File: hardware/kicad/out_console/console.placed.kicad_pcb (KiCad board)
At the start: 2 copper layers, 115 x 96 mm, 53 parts, among them J1 RaspberryPi_Pico_SMD_HandSold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, J10 JST_XH_B2B-XH-A_1x02_P2.50mm_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, J11 JST_XH_B2B-XH-A_1x02_P2.50mm_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, J12 JST_XH_B2B-XH-A_1x02_P2.50mm_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, J13 JST_XH_B2B-XH-A_1x02_P2.50mm_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, J14 JST_XH_B2B-XH-A_1x02_P2.50mm_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, J15 JST_XH_B2B-XH-A_1x02_P2.50mm_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, J16 JST_XH_B2B-XH-A_1x02_P2.50mm_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, J17 JST_XH_B2B-XH-A_1x02_P2.50mm_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, J18 JST_XH_B2B-XH-A_1x02_P2.50mm_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, J19 JST_XH_B2B-XH-A_1x02_P2.50mm_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, J2 IDC-Header_2x20_P2.54mm_Verti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, J20 JST_XH_B3B-XH-A_1x03_P2.50mm_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, J21 JST_XH_B3B-XH-A_1x03_P2.50mm_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, J22 PinHeader_2x04_P2.54mm_Vertic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, J3 JST_XH_B4B-XH-A_1x04_P2.50mm_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, J4 JST_XH_B3B-XH-A_1x03_P2.50mm_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, J5 JST_XH_B2B-XH-A_1x02_P2.50mm_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, J6 JST_XH_B8B-XH-A_1x08_P2.50mm_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, J7 JST_XH_B3B-XH-A_1x03_P2.50mm_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, J8 JST_XH_B2B-XH-A_1x02_P2.50mm_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, U1 DIP-14_W7.62mm, U2 DIP-6_W7.62mm

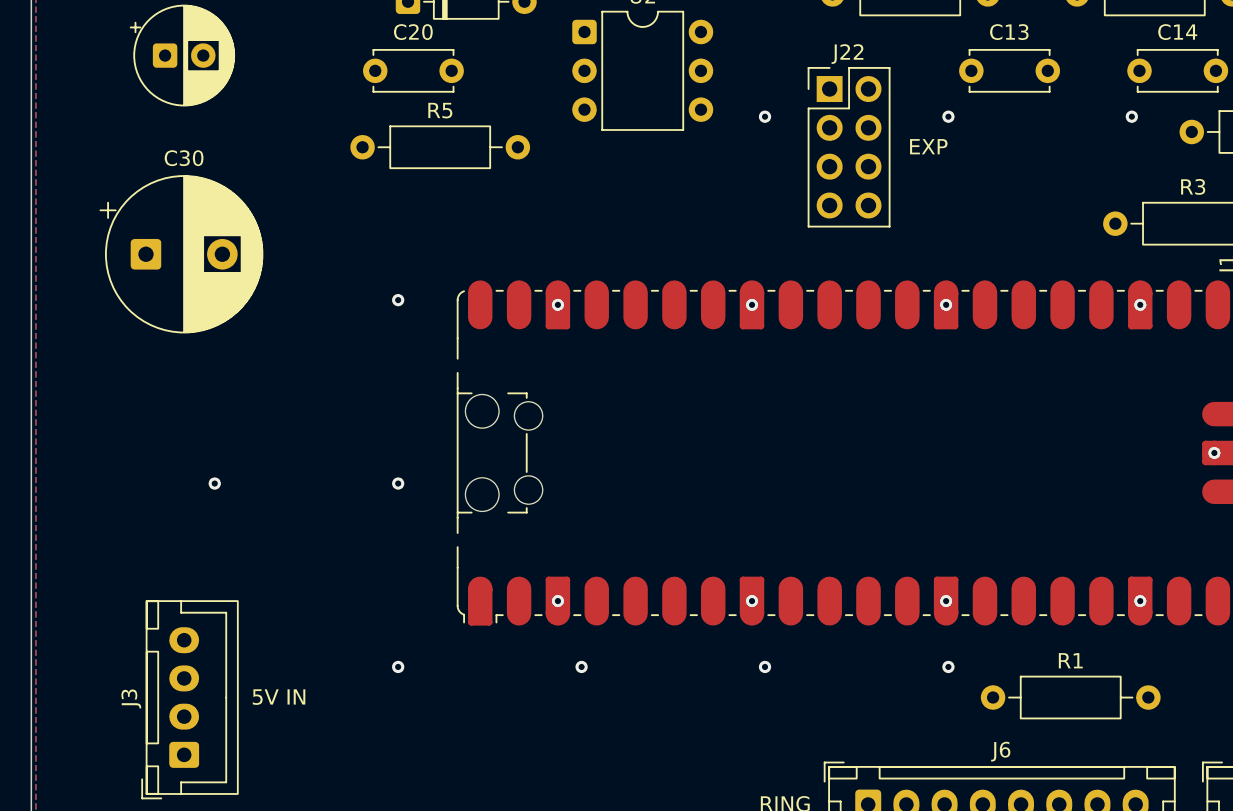
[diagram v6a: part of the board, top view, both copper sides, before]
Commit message: fix(hardware): the four electrical blockers from the pre-fab review
- ENCODER LEVELS. ring_board.py pulled ENC_A/ENC_B up to its 5 V rail; those land
  on GP13/GP14, whose absolute maximum is 3.6 V. Correct when the far end was
  main_board.py's 5 V Pro Micro, wrong from the day it became a Pico. The pull-ups
  move to this board at 3V3 (and ENC_SW gains the one it never had). New
  PICO_LEVELS gate: PI_LEVELS only ever guarded the Pi, so no check on either
  board could see this.
- PI 5 V. Header pins 2/4 are no longer connected. Tying them put the external
  buck in hard parallel with the Pi 5's PMIC rail with no ORing diode, and after
  the rail merge it put the whole WS2812 load on the Pi's 5 V pin -- which
  segno_console_shopping_list.md forbids in as many words. Gated.
- POWER BUTTON. GPIO3 wakes a Pi 4, not a Pi 5, where the GPIO sits behind RP1
  and the PMIC owns power-on. The button passes through to the Pi's own J2 solder
  pads via J9. The old gate asserted the false version and enforced it all design.
- CTRL REFERENCE. One 1k per jack, not one shared. Shared, a TS footswitch in
  either jack pulled the other jack's pot top to ground.

Also: track width 0.2 -> 0.6 mm (Freerouting reads widths from the DSN netclass,
so TRACK_W/TRACK_PWR were decorative and +5V carried ~1 A on 0.5 A copper);
export() refuses to plot a board with no tracks; --severity-all everywhere.

Refs #747
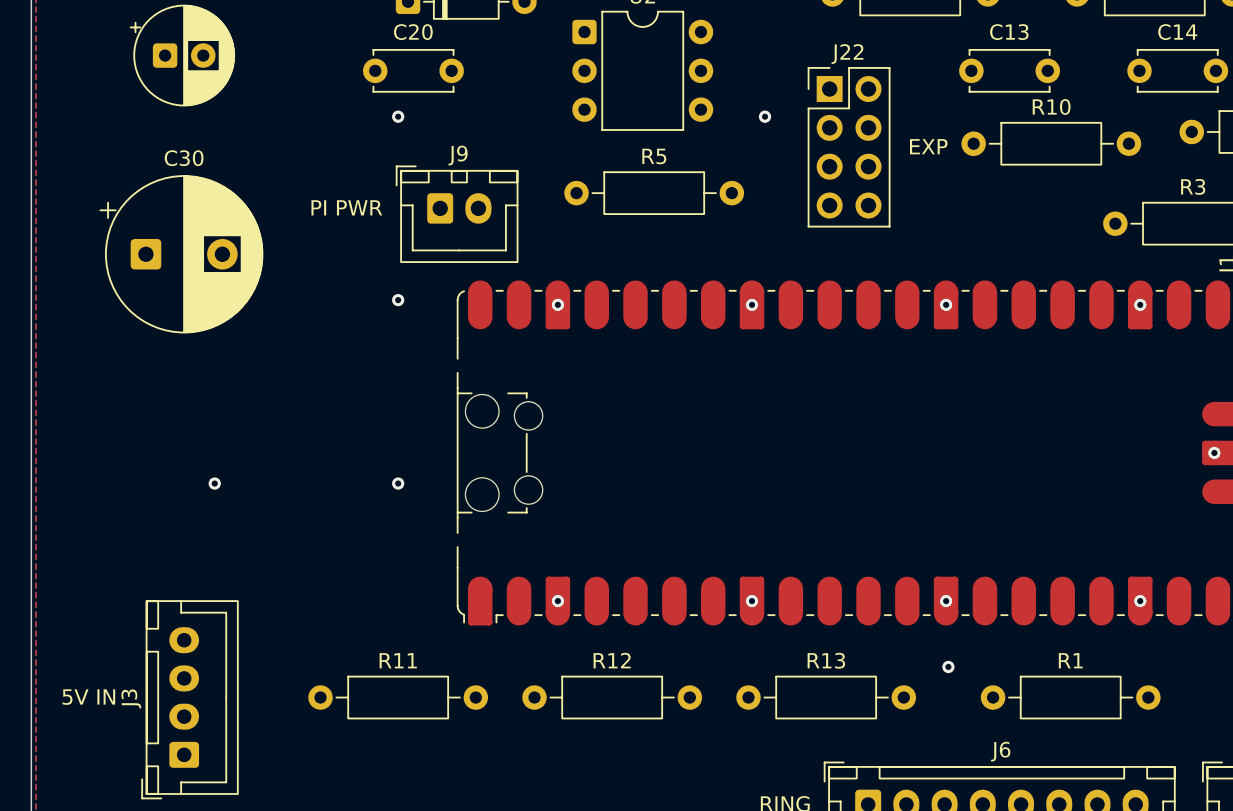
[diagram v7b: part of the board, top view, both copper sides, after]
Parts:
- added J9: JST_XH_B2B-XH-A_1x02_P2.50mm_Vertical, JST_XH_B2B-XH-A_1x02_P2.50mm_Vertical, F.Cu at (126.8, 90.0)
- added R10: R_Axial_DIN0207_L6.3mm_D2.5mm_P10.16mm_Horizontal, R_Axial_DIN0207_L6.3mm_D2.5mm_P10.16mm_Horizontal, F.Cu at (161.7, 85.8)
- added R11: R_Axial_DIN0207_L6.3mm_D2.5mm_P10.16mm_Horizontal, R_Axial_DIN0207_L6.3mm_D2.5mm_P10.16mm_Horizontal, F.Cu at (118.9, 122.0)
- added R12: R_Axial_DIN0207_L6.3mm_D2.5mm_P10.16mm_Horizontal, R_Axial_DIN0207_L6.3mm_D2.5mm_P10.16mm_Horizontal, F.Cu at (132.9, 122.0)
- added R13: R_Axial_DIN0207_L6.3mm_D2.5mm_P10.16mm_Horizontal, R_Axial_DIN0207_L6.3mm_D2.5mm_P10.16mm_Horizontal, F.Cu at (146.9, 122.0)
- moved R5 14.3 mm to (135.7, 89.0)
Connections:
- J2 pad 2: +5V -> (no net)
- J2 pad 4: +5V -> (no net)
- J2 pad 5: PWR_BTN -> (no net)
- J20 pad 2: CTRL_REF -> J20_REF
- J21 pad 2: CTRL_REF -> J21_REF
- R7 pad 2: CTRL_REF -> J20_REF
- R9 pad 2: CTRL2_TIP -> J21_REF
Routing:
- net GND: vias 84 -> 81
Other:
- board text added: "PI PWR"

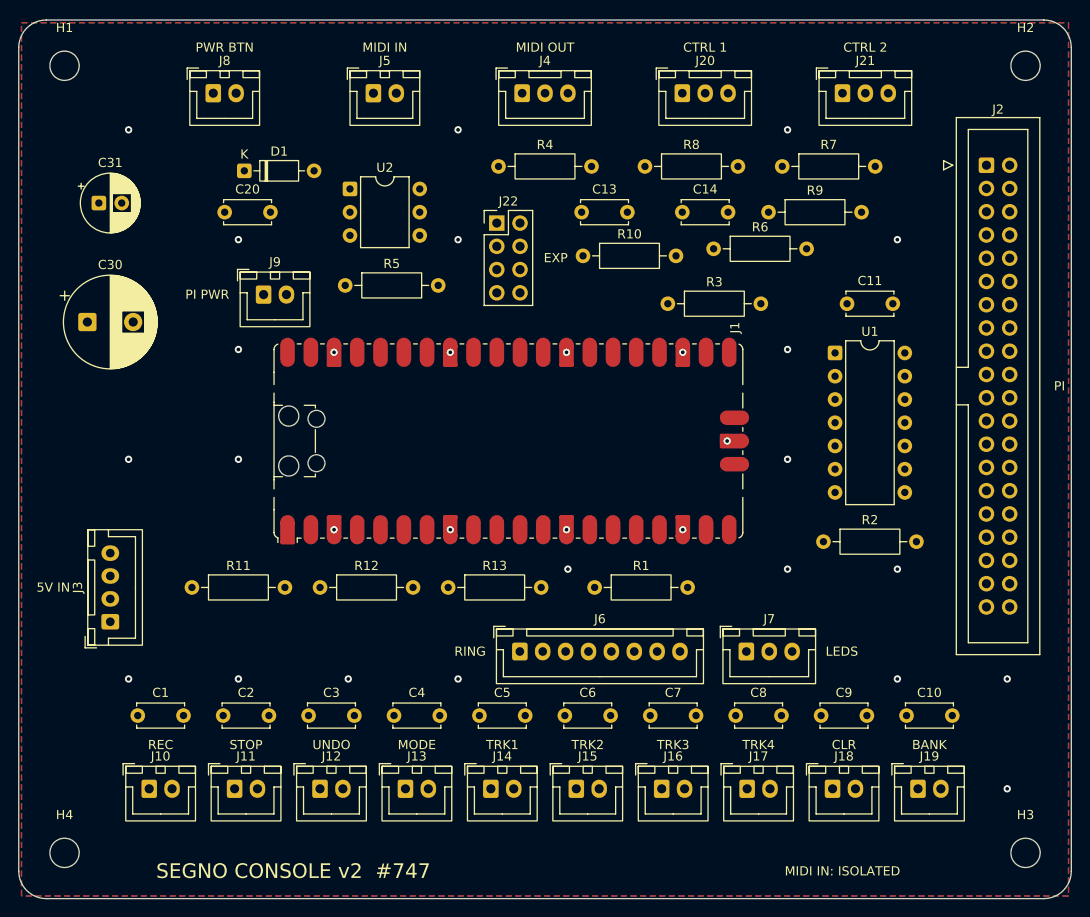
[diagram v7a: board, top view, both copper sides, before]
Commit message: fix(hardware): the console board comes back DRC-clean
133 violations to 0, with 0 unconnected, on three consecutive routing runs
that each found a different solution -- so it is the board that is clean,
not one lucky roll of the autorouter.

102 holes_co_located: every one was a stitching via sitting dead on the
centre of a plated through-hole pad, put there by _stitch_gnd(), which
dropped a via on every GND pad without asking what kind of pad it was. A
plated hole already joins both layers, so those vias connected nothing and
only asked CAM to drill the same coordinate twice. Vias now go BESIDE the
pad -- offset toward the part's own body, since a pad's fan-out leaves
outward and a via in that lane cost SW_TRACK3 its route -- with a stub
back to the pad, and a keepout list of every pad on the board that the
blind lattice is also checked against.

31 via_dangling: lattice vias left in pour islands the fill deleted. That
cannot be known at placement time, because the fill happens after routing,
so it is no longer guessed: --prune-vias pours, asks DRC which vias are
dangling, deletes exactly those, and repeats until a pour comes back with
none. route_console_board.sh runs it after the SES import.

14 silk_overlap: the pinned label rows never entered the occupancy list,
so all ten footswitch designators were placed 0.07 mm from their own
labels. Labels are now measured as rendered rather than estimated from
character counts, and the gate checks silk against silk as well.

Two starved_thermal at J6 were the same problem as the dangling vias seen
from the other end: the lattice cannot place a via near a connector, so
the pour fragments exactly where the headers are. Tying every GND pad
fixes both; an 8 mm lattice was tried first and is the wrong lever, since
it does not reach the connectors either and its extra obstacles in the
open middle left SWCLK unrouted.

Gates that could not fail, found by the same audit:

- THERMALS ran before the pours existed, so it looped over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
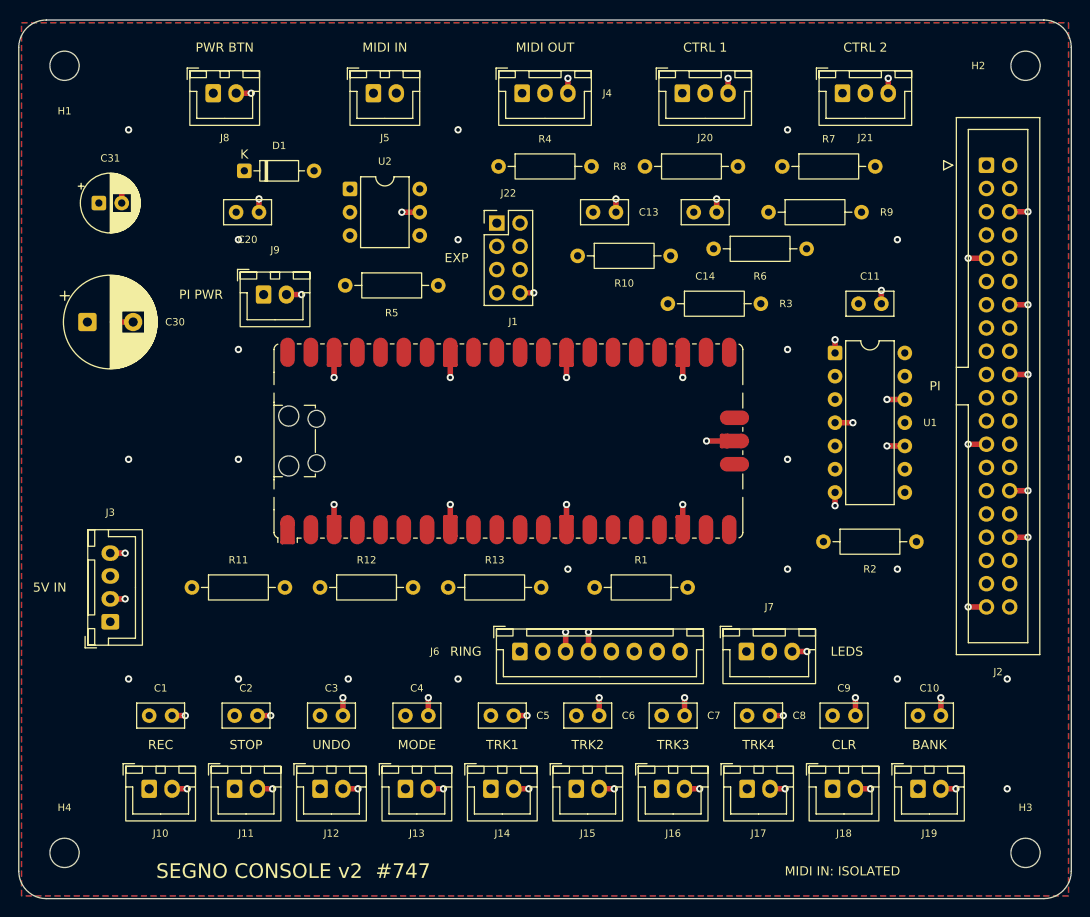
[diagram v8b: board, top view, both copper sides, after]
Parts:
- C1, C10, C11, C13, C14, C2, C20, C3, C4, C5, C6, C7, C8, C9: value C_Disc_D5.0mm_W2.5mm_P5.00mm -> C_Disc_D5.0mm_W2.5mm_P2.50mm; footprint C_Disc_D5.0mm_W2.5mm_P5.00mm -> C_Disc_D5.0mm_W2.5mm_P2.50mm
- moved C1 1.25 mm to (114.2, 136.0)
- moved C10 1.25 mm to (198.2, 136.0)
- moved C11 1.25 mm to (191.8, 91.0)
- moved C13 1.25 mm to (162.8, 81.0)
- moved C14 1.25 mm to (173.8, 81.0)
- moved C2 1.25 mm to (123.6, 136.0)
- moved C20 1.25 mm to (123.8, 81.0)
- moved C3 1.25 mm to (132.9, 136.0)
- moved C4 1.25 mm to (142.2, 136.0)
- moved C5 1.25 mm to (151.6, 136.0)
- moved C6 1.25 mm to (160.9, 136.0)
- moved C7 1.25 mm to (170.2, 136.0)
- moved C8 1.25 mm to (179.6, 136.0)
- moved C9 1.25 mm to (188.9, 136.0)
- moved R10 0.58 mm to (161.1, 85.8)
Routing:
- net GND: track 0.00 -> 113.1 mm
